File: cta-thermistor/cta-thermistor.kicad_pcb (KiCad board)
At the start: 2 copper layers, 91.4 x 86.4 mm, 42 parts, among them Con1 100u, Q1 TIP120, Q2 BC557, U1 OP07, U2 LM358

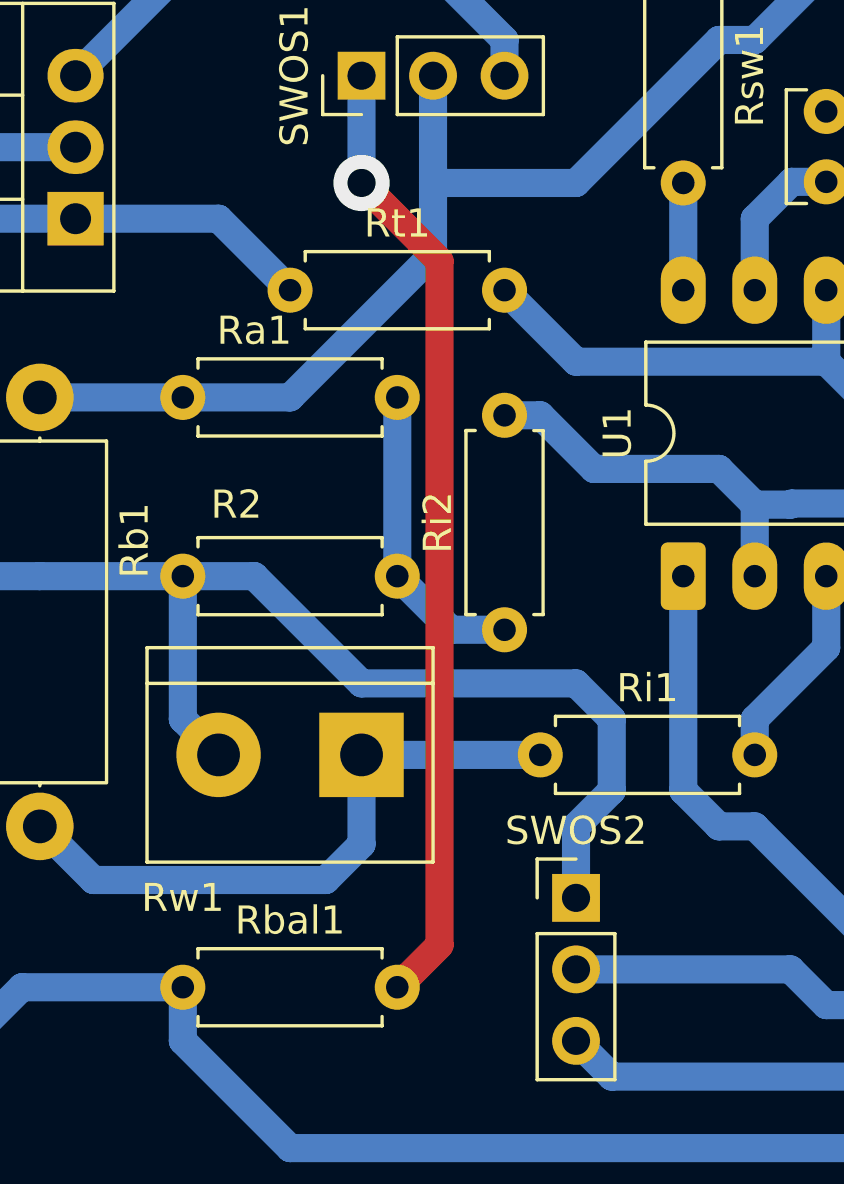
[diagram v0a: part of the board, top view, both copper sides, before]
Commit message: Small change. A via was on a PTH resistor
Not wrong but kind of annoying when you are making the PCB by hand.
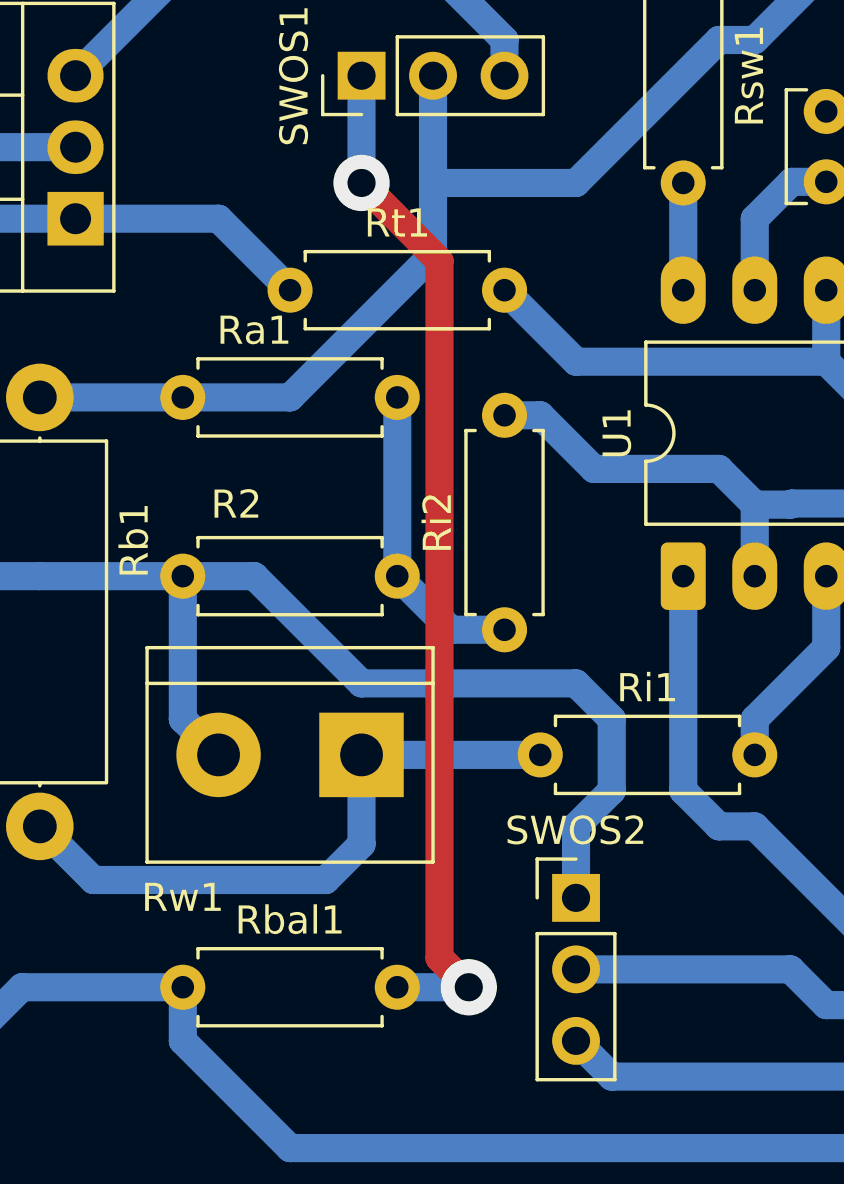
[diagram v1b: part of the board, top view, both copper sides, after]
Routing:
- net Net-(SWOS1-A): track 34.2 -> 36.5 mm, vias 1 -> 2
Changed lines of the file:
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@@
 	(segment
 		(start 138.661 78.971)
-		(end 135.89 76.2)
+		(end 138.661 103.736)
 		(width 1)
 		(layer "F.Cu")
@@
 	)
 	(segment
-		(start 137.16 104.775)
-		(end 138.661 103.274)
+		(start 135.89 76.2)
+		(end 138.661 78.971)
 		(width 1)
 		(layer "F.Cu")
@@
 	)
 	(segment
-		(start 138.661 103.274)
-		(end 138.661 78.971)
+		(start 138.661 103.736)
+		(end 139.7 104.775)
 		(width 1)
 		(layer "F.Cu")
+		(net 20)
+	)
+	(via
+		(at 139.7 104.775)
+		(size 2)
+		(drill 1)
+		(layers "F.Cu" "B.Cu")
 		(net 20)
 	)
@@
 		(width 1)
 		(layer "B.Cu")
+		(net 20)
+	)
+	(segment
+		(start 137.16 104.775)
+		(end 139.7 104.775)
+		(width 1)
+		(layer "B.Cu")

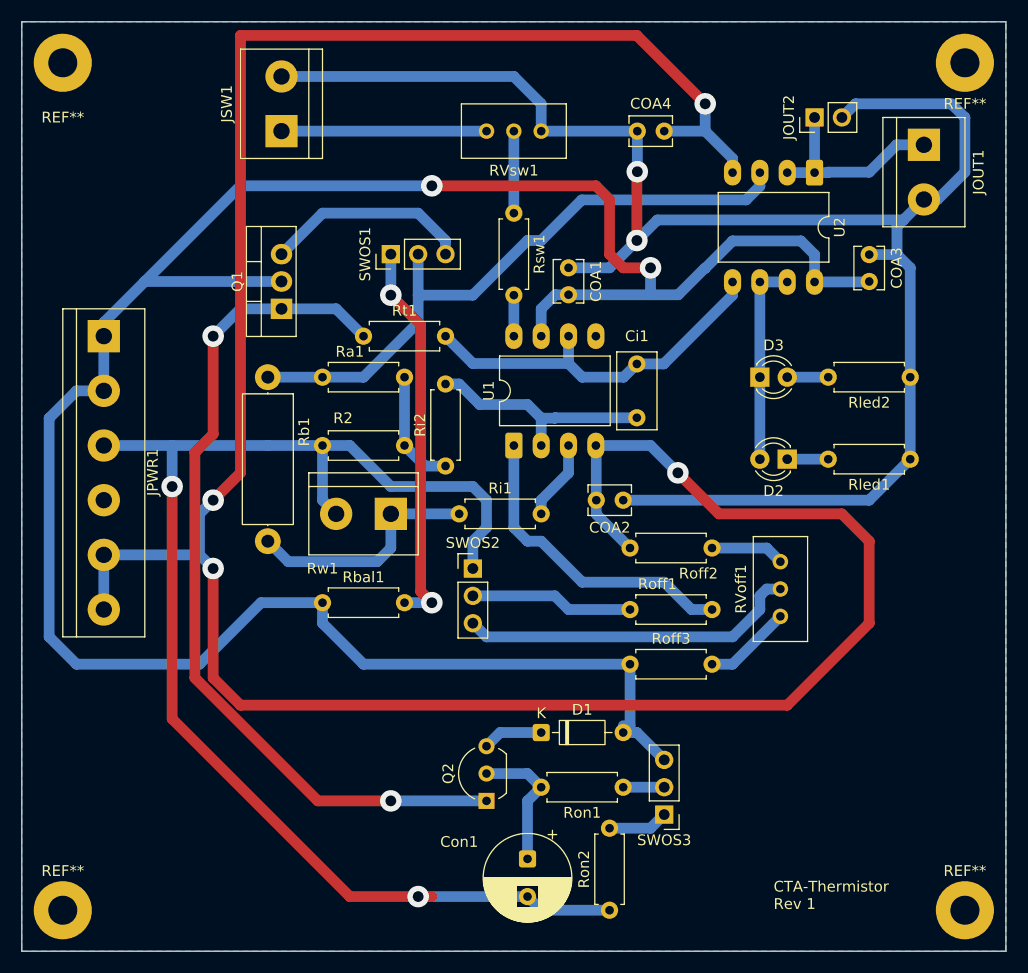
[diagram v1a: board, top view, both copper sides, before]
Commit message: I used the wrong footprint for the OpAmps
I mistakenly selected a wide footprint. Used the opportunity to do some improvements on the PCB layout.
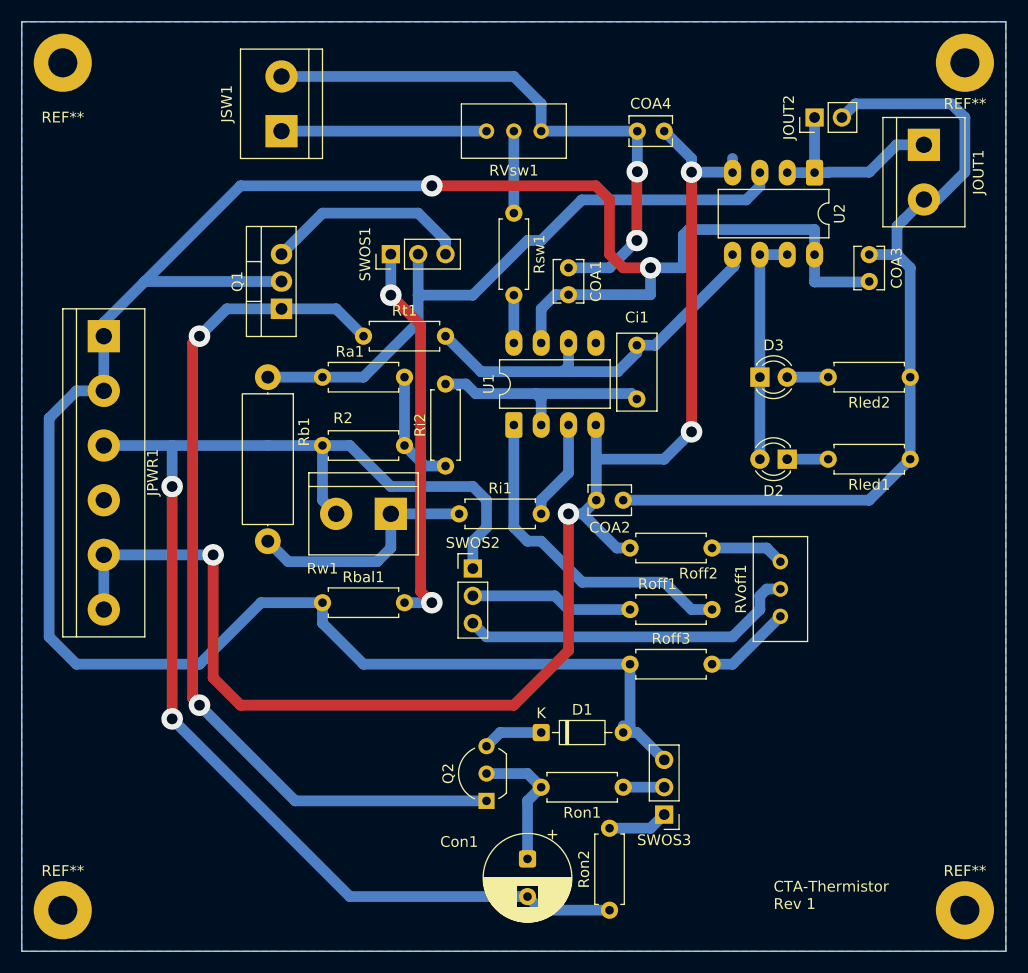
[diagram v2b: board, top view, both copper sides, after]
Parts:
- U1, U2: footprint Package_DIP:DIP-8_W10.16mm_LongPads -> Package_DIP:DIP-8_W7.62mm_LongPads
- moved U1 1.91 mm to (147.3, 88.3)
- moved Ci1 1.74 mm to (158.8, 85.9)
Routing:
- net VEE: track 245.5 -> 135.4 mm
- net GND: track 284.9 -> 258.0 mm
- net VCC: track 221.9 -> 225.5 mm
- net Net-(D2-A): track 19.0 -> 21.5 mm
- net /Von: track 80.4 -> 82.5 mm
- net Net-(U1-+): track 7.40 -> 9.31 mm
- net /Off: track 29.2 -> 31.1 mm
- net /OPout: track 35.2 -> 36.7 mm
- net /SW: track 3.81 -> 4.44 mm
